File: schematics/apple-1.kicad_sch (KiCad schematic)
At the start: 9 parts, among them SW1 SW_Push, U1 W65C02SxP, U2 28C256, U3 74HC138, U4 CY62256-70PC, U5 W65C21SxP, U6 74HC04

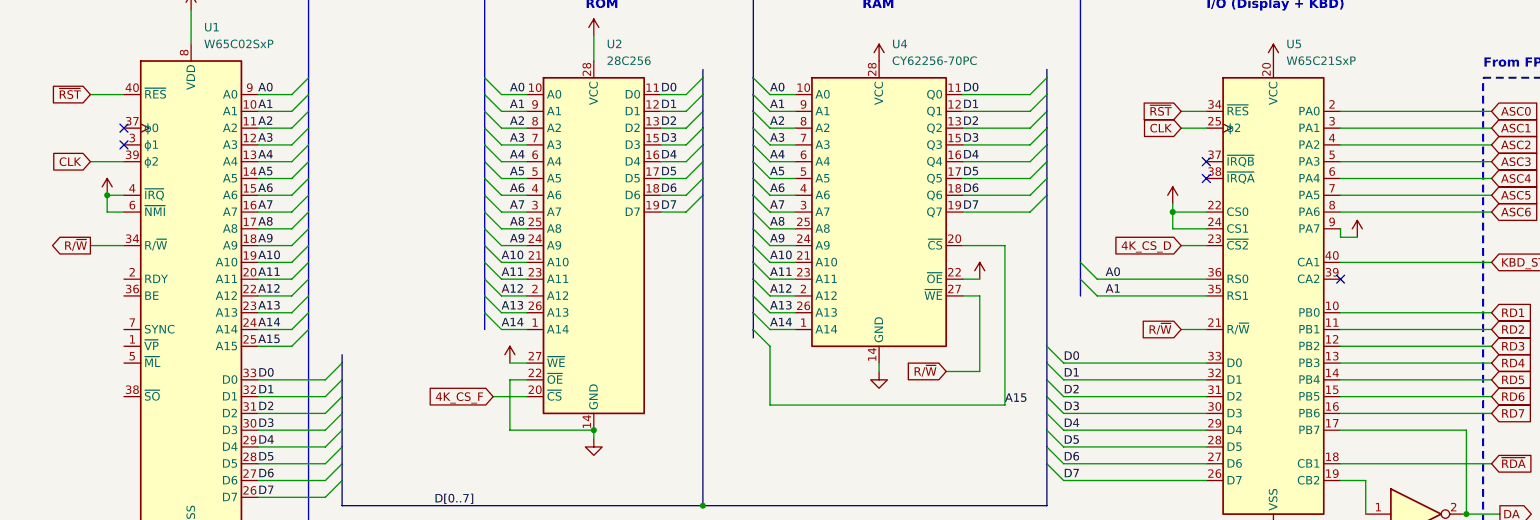
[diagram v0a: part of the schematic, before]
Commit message: updated schematics
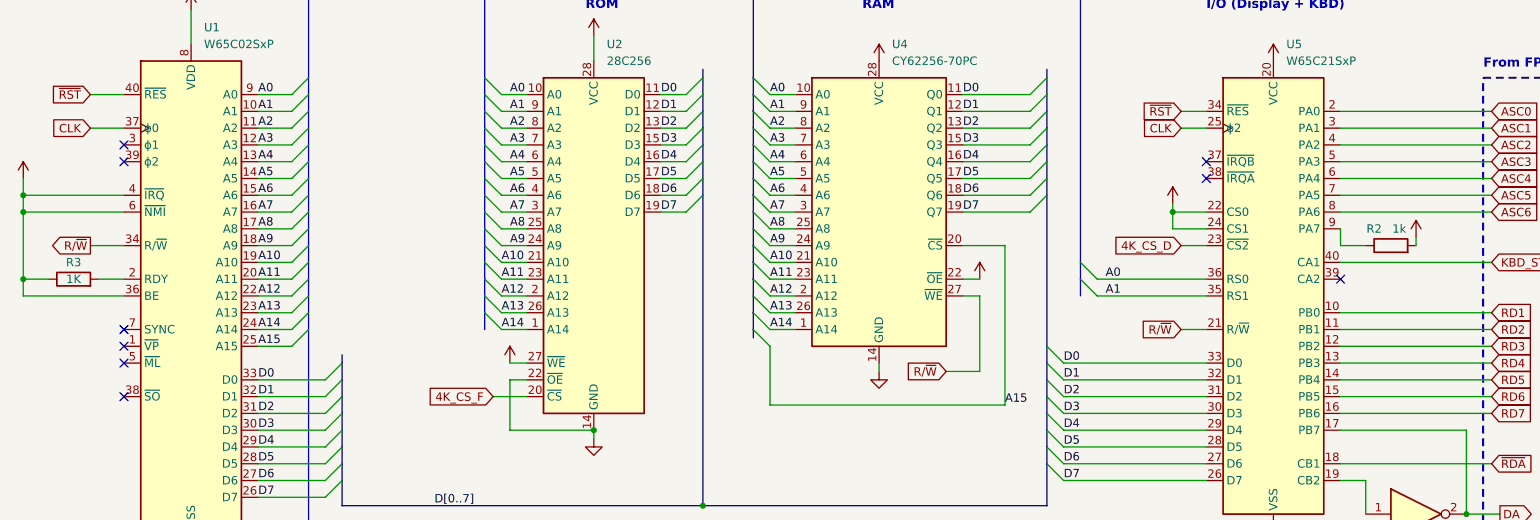
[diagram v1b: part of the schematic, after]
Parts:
- added R2: 1k, symbol Device:R
- added R3: 1K, symbol Device:R
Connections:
- net CLK: now also U1.37 (ϕ0); no longer U1.39 (ϕ2)
- net VCC: now also U1.36 (BE), R2.2, R3.1; no longer U5.9 (PA7)
- net at U1.2 (RDY): now also R3.2
- new net: R2.1, U5.9 (PA7)
- no-connect marks 5 -> 9

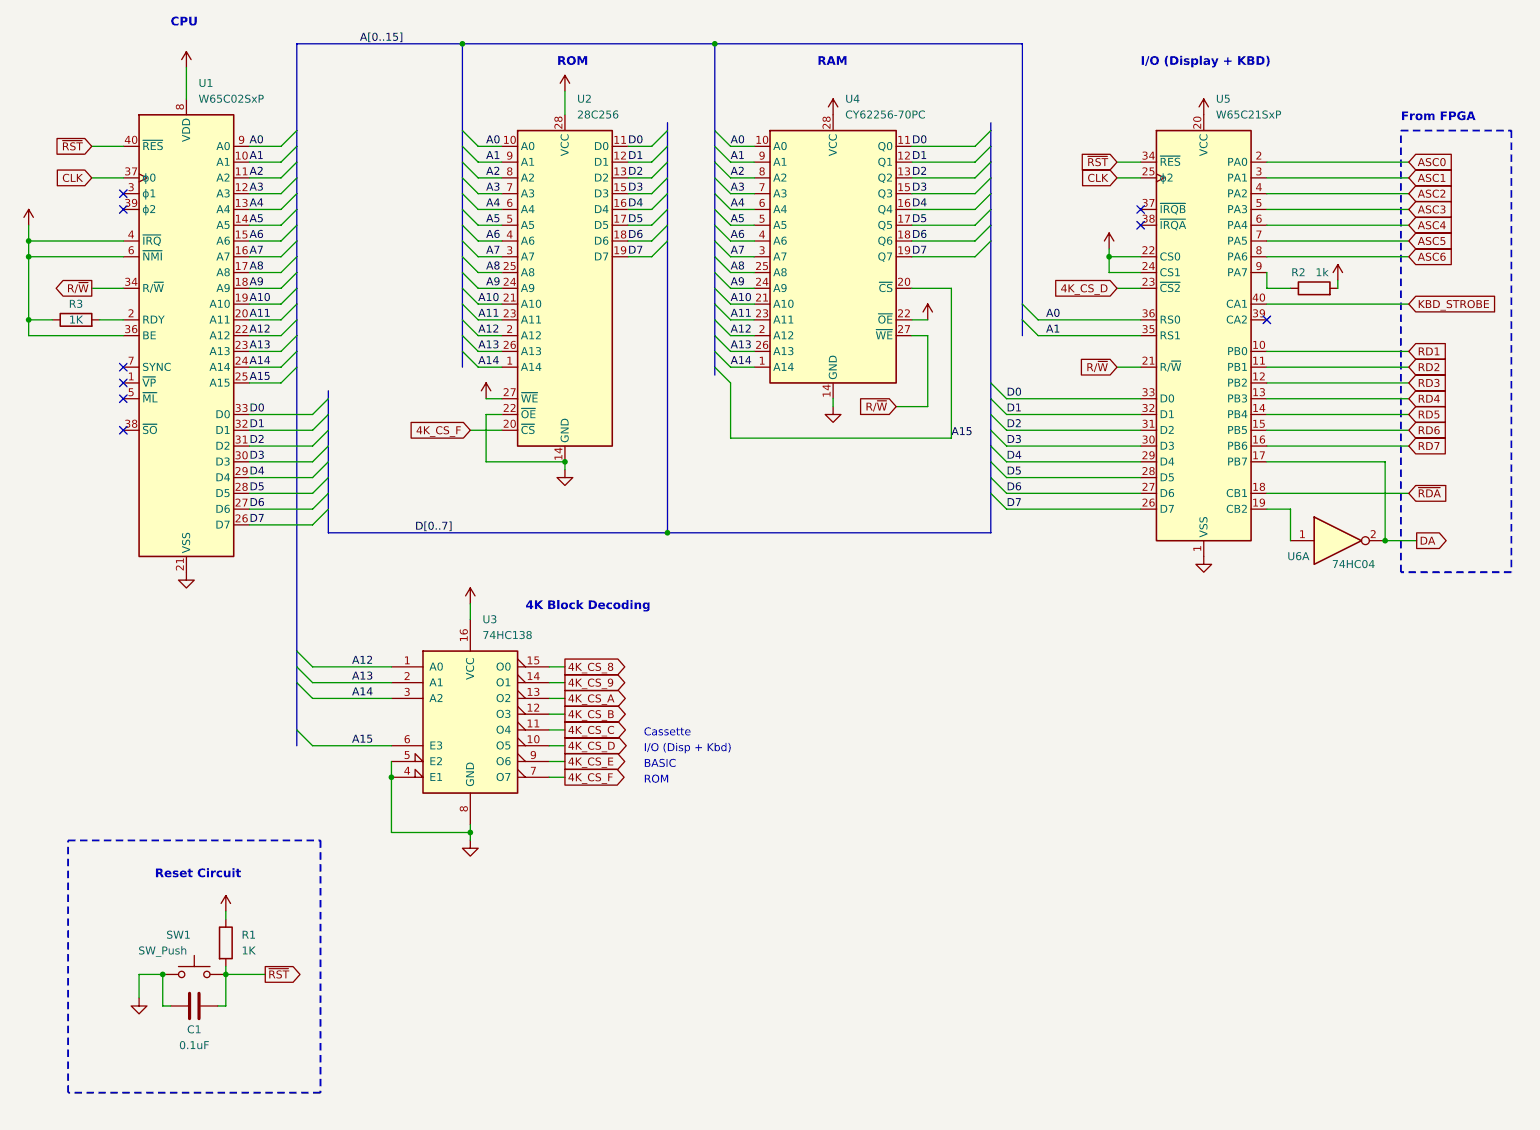
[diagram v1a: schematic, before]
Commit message: added first batch of ACI files
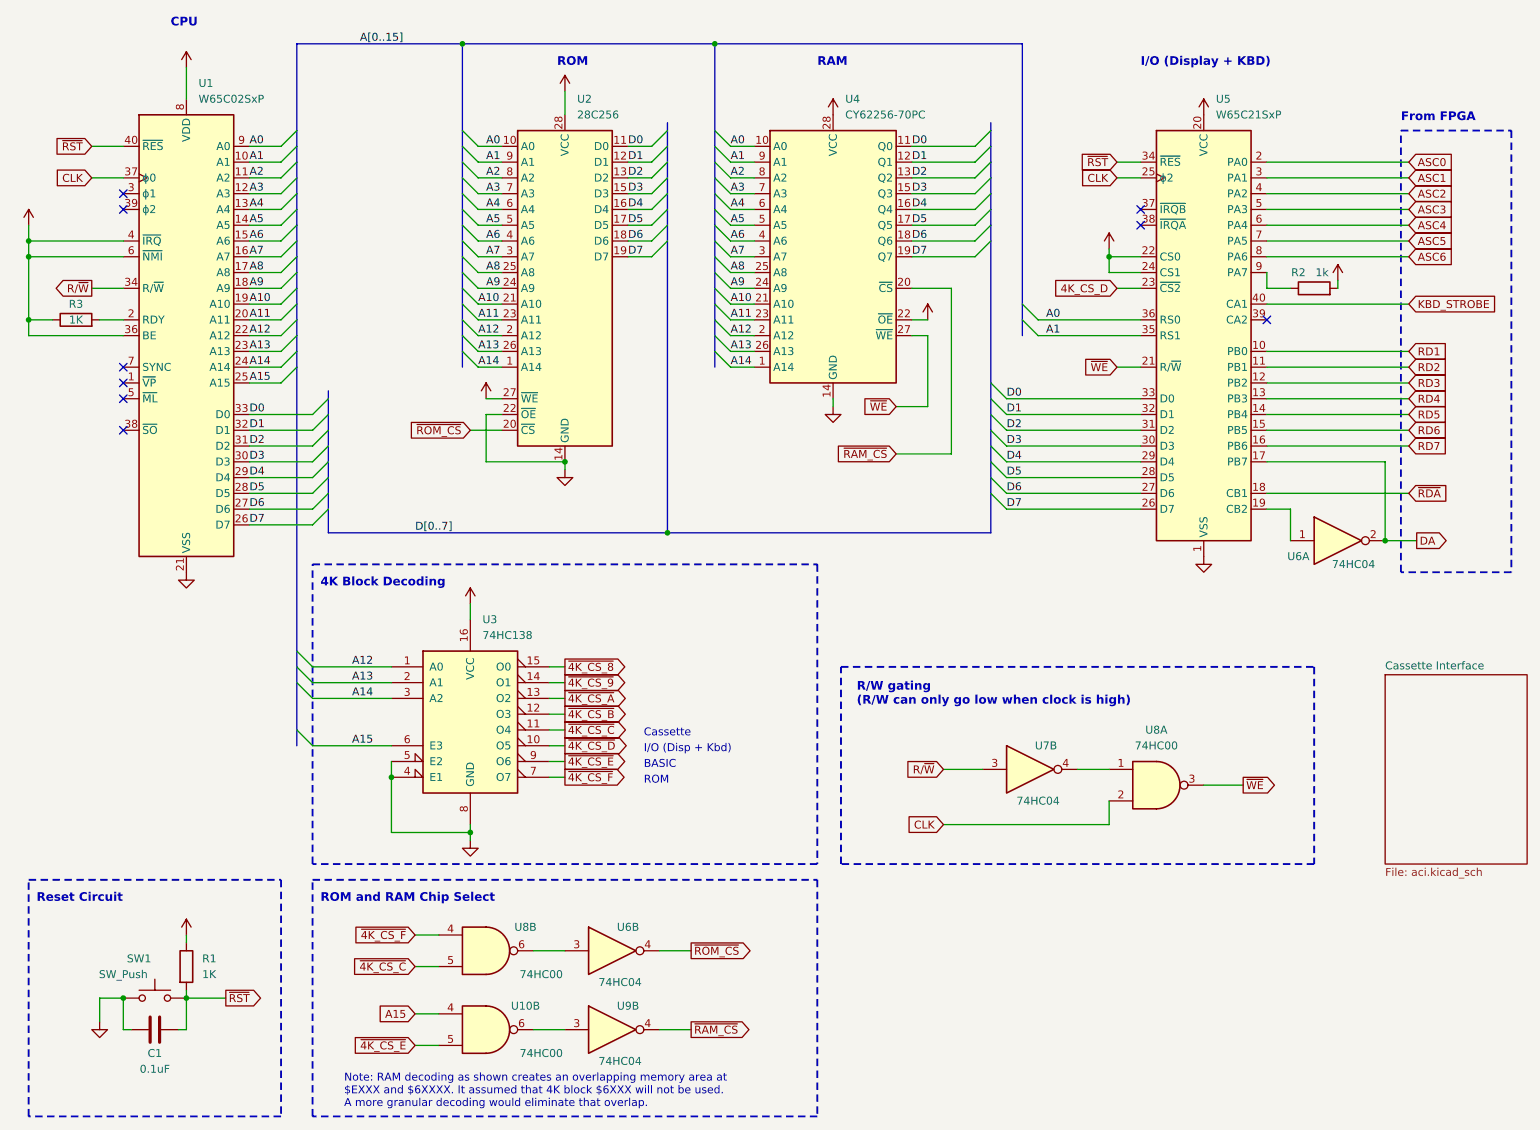
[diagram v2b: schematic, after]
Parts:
- added U10, U8: 74HC00, symbol 74xx:74HC00
- added unit 2 of U6
- added U7, U9: 74HC04, symbol 74xx:74HC04
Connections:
- net 4K_CS_D: no longer U3.10 (O5)
- net A15: now also U10.4; no longer U4.20 (~{CS})
- net CLK: now also U8.2
- net R/~{W}: now also U7.3; no longer U4.27 (~{WE}), U5.21 (R/~{W})
- net 4K_CS_8 renamed ~{4K_CS_8}
- net 4K_CS_9 renamed ~{4K_CS_9}
- net 4K_CS_A renamed ~{4K_CS_A}
- net 4K_CS_B renamed ~{4K_CS_B}
- net 4K_CS_C renamed ~{4K_CS_C}
- net ~{4K_CS_C}: now also U8.5
- net 4K_CS_E renamed ~{4K_CS_E}
- net ~{4K_CS_E}: now also U10.5
- net 4K_CS_F renamed ~{4K_CS_F}
- net ~{4K_CS_F}: now also U8.4; no longer U2.20 (~{CS})
- new net: U10.6, U9.3
- new net: U7.4, U8.1
- new net: U6.3, U8.6
- new net ~{4K_CS_D}: U3.10 (O5)
- new net ~{RAM_CS}: U4.20 (~{CS}), U9.4
- new net ~{ROM_CS}: U2.20 (~{CS}), U6.4
- new net ~{WE}: U4.27 (~{WE}), U5.21 (R/~{W}), U8.3
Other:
- added sheet Cassette Interface (aci.kicad_sch)
- note added: "Note: RAM decoding as shown creates an overlapping memory area at $EXXX and $6XXXX. It assumed that 4K block $6XXX will not be used. A more granular decoding would eliminate that overlap."
- note added: "R/W gating (R/W can only go low when clock is high)"
- note added: "ROM and RAM Chip Select"
- moved on the sheet: C1, R1, SW1

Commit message: added UART to design
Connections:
- net GND: no longer U2.22 (~{OE})
- net ~{R}/W: now reaches U7.4, U8.1
- net ~{R}/W: now also U2.22 (~{OE})
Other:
- added sheet IEC Interface (iec_interface.kicad_sch)
- added sheet UART (uart.kicad_sch)
- added sheet UART-FPGA (uart-fpga.kicad_sch)
- note added: "Apple 1 on Breadboard Project"
- note added: "I/O IEC Disk"
- moved on the sheet: U7B, U8A
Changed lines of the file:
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@@
   (junction (at 43.18 180.34) (diameter 0) (color 0 0 0 0)
   )
+  (junction (at 189.23 147.32) (diameter 0) (color 0 0 0 0)
+  )
   (junction (at 236.22 106.68) (diameter 0) (color 0 0 0 0)
-  )
-  (junction (at 104.14 93.98) (diameter 0) (color 0 0 0 0)
   )
   (junction (at 33.02 180.34) (diameter 0) (color 0 0 0 0)
@@
     (stroke (width 0) (type default))
   )
+  (wire (pts (xy 189.23 137.16) (xy 189.23 147.32))
+    (stroke (width 0) (type default))
+  )
   (wire (pts (xy 217.17 83.82) (xy 240.03 83.82))
     (stroke (width 0) (type default))
@@
     (stroke (width 0) (type default))
   )
-  (wire (pts (xy 93.98 86.36) (xy 91.44 86.36))
+  (wire (pts (xy 88.9 86.36) (xy 93.98 86.36))
     (stroke (width 0) (type default))
   )
@@
     (stroke (width 0) (type default))
   )
-  (wire (pts (xy 165.1 152.4) (xy 191.77 152.4))
+  (wire (pts (xy 165.1 156.21) (xy 191.77 156.21))
     (stroke (width 0) (type default))
   )
@@
     (stroke (width 0) (type default))
   )
+  (wire (pts (xy 191.77 137.16) (xy 189.23 137.16))
+    (stroke (width 0) (type default))
+  )
   (bus (pts (xy 66.04 86.36) (xy 66.04 88.9))
     (stroke (width 0) (type default))
@@
     (stroke (width 0) (type default))
   )
-  (wire (pts (xy 207.01 146.05) (xy 213.36 146.05))
+  (wire (pts (xy 207.01 149.86) (xy 213.36 149.86))
     (stroke (width 0) (type default))
   )
@@
     (stroke (width 0) (type default))
   )
-  (wire (pts (xy 191.77 152.4) (xy 191.77 148.59))
+  (wire (pts (xy 191.77 156.21) (xy 191.77 152.4))
     (stroke (width 0) (type default))
   )
@@
     (stroke (width 0) (type default))
   )
-  (wire (pts (xy 91.44 93.98) (xy 104.14 93.98))
-    (stroke (width 0) (type default))
-  )
   (wire (pts (xy 130.81 55.88) (xy 134.62 55.88))
     (stroke (width 0) (type default))
@@
     (stroke (width 0) (type default))
   )
-  (wire (pts (xy 91.44 86.36) (xy 91.44 93.98))
-    (stroke (width 0) (type default))
-  )
   (wire (pts (xy 130.81 50.8) (xy 134.62 50.8))
     (stroke (width 0) (type default))
@@
     (stroke (width 0) (type default))
   )
-  (wire (pts (xy 186.69 143.51) (xy 191.77 143.51))
+  (wire (pts (xy 186.69 147.32) (xy 189.23 147.32))
     (stroke (width 0) (type default))
   )
@@
     (stroke (width 0) (type default))
   )
-  (wire (pts (xy 165.1 143.51) (xy 171.45 143.51))
+  (wire (pts (xy 165.1 147.32) (xy 171.45 147.32))
     (stroke (width 0) (type default))
   )
@@
   )
   (bus (pts (xy 172.72 96.52) (xy 172.72 99.06))
+    (stroke (width 0) (type default))
+  )
+  (wire (pts (xy 189.23 147.32) (xy 191.77 147.32))
     (stroke (width 0) (type default))
   )
@@
     (fill (type none))
   )
+  (text "Apple 1 on Breadboard Project" (at 240.03 181.61 0)
+    (effects (font (size 2.54 2.54) (thickness 0.508) bold) (justify right bottom))
+  )
   (text "BASIC" (at 116.84 143.51 0)
+    (effects (font (size 1.27 1.27)) (justify left bottom))
+  )
+  (text "I/O IEC Disk" (at 116.84 135.89 0)
     (effects (font (size 1.27 1.27)) (justify left bottom))
   )
@@
     )
   )
-  (global_label "R{slash}~{W}" (shape input) (at 165.1 143.51 180) (fields_autoplaced)
+  (global_label "R{slash}~{W}" (shape input) (at 165.1 147.32 180) (fields_autoplaced)
     (effects (font (size 1.27 1.27)) (justify right))
-    (property "Intersheetrefs" "${INTERSHEET_REFS}" (at 158.1423 143.51 0)
+    (property "Intersheetrefs" "${INTERSHEET_REFS}" (at 158.1423 147.32 0)
       (effects (font (size 1.27 1.27)) (justify right) hide)
     )
@@
     )
   )
-  (global_label "~{WE}" (shape output) (at 213.36 146.05 0) (fields_autoplaced)
-    (effects (font (size 1.27 1.27)) (justify left))
-    (property "Intersheetrefs" "${INTERSHEET_REFS}" (at 218.8662 146.05 0)
+  (global_label "~{WE}" (shape output) (at 213.36 149.86 0) (fields_autoplaced)
+    (effects (font (size 1.27 1.27)) (justify left))
+    (property "Intersheetrefs" "${INTERSHEET_REFS}" (at 218.8662 149.86 0)
       (effects (font (size 1.27 1.27)) (justify left) hide)
     )
@@
     )
   )
-  (global_label "CLK" (shape input) (at 165.1 152.4 180) (fields_autoplaced)
+  (global_label "CLK" (shape input) (at 165.1 156.21 180) (fields_autoplaced)
     (effects (font (size 1.27 1.27)) (justify right))
-    (property "Intersheetrefs" "${INTERSHEET_REFS}" (at 158.6261 152.4 0)
+    (property "Intersheetrefs" "${INTERSHEET_REFS}" (at 158.6261 156.21 0)
       (effects (font (size 1.27 1.27)) (justify right) hide)
     )
@@
     (effects (font (size 1.27 1.27)) (justify left))
     (property "Intersheetrefs" "${INTERSHEET_REFS}" (at 115.1495 127 0)
+      (effects (font (size 1.27 1.27)) (justify left) hide)
+    )
+  )
+  (global_label "~{R}{slash}W" (shape output) (at 191.77 137.16 0) (fields_autoplaced)
+    (effects (font (size 1.27 1.27)) (justify left))
+    (property "Intersheetrefs" "${INTERSHEET_REFS}" (at 198.7277 137.16 0)
       (effects (font (size 1.27 1.27)) (justify left) hide)
     )
@@
     (effects (font (size 1.27 1.27)) (justify right))
     (property "Intersheetrefs" "${INTERSHEET_REFS}" (at 20.9823 66.04 0)
+      (effects (font (size 1.27 1.27)) (justify right) hide)
+    )
+  )
+  (global_label "~{R}{slash}W" (shape input) (at 88.9 86.36 180) (fields_autoplaced)
+    (effects (font (size 1.27 1.27)) (justify right))
+    (property "Intersheetrefs" "${INTERSHEET_REFS}" (at 81.9423 86.36 0)
       (effects (font (size 1.27 1.27)) (justify right) hide)
     )
@@
     )
   )
-  (symbol (lib_id "74xx:74HC00") (at 199.39 146.05 0) (unit 1)
+  (symbol (lib_id "74xx:74HC00") (at 199.39 149.86 0) (unit 1)
     (in_bom yes) (on_board yes) (dnp no) (fields_autoplaced)
-    (property "Reference" "U8" (at 199.3817 137.16 0)
+    (property "Reference" "U8" (at 199.3817 140.97 0)
       (effects (font (size 1.27 1.27)))
     )
-    (property "Value" "74HC00" (at 199.3817 139.7 0)
+    (property "Value" "74HC00" (at 199.3817 143.51 0)
       (effects (font (size 1.27 1.27)))
     )
-    (property "Footprint" "" (at 199.39 146.05 0)
-      (effects (font (size 1.27 1.27)) hide)
-    )
-    (property "Datasheet" "http://www.ti.com/lit/gpn/sn74hc00" (at 199.39 146.05 0)
+    (property "Footprint" "" (at 199.39 149.86 0)
+      (effects (font (size 1.27 1.27)) hide)
+    )
+    (property "Datasheet" "http://www.ti.com/lit/gpn/sn74hc00" (at 199.39 149.86 0)
       (effects (font (size 1.27 1.27)) hide)
     )
@@
     )
   )
-  (symbol (lib_id "74xx:74HC04") (at 179.07 143.51 0) (unit 2)
+  (symbol (lib_id "74xx:74HC04") (at 179.07 147.32 0) (unit 2)
     (in_bom yes) (on_board yes) (dnp no)
-    (property "Reference" "U7" (at 181.61 139.7 0)
+    (property "Reference" "U7" (at 181.61 143.51 0)
       (effects (font (size 1.27 1.27)))
     )
-    (property "Value" "74HC04" (at 180.34 148.59 0)
+    (property "Value" "74HC04" (at 180.34 152.4 0)
       (effects (font (size 1.27 1.27)))
     )
-    (property "Footprint" "" (at 179.07 143.51 0)
-      (effects (font (size 1.27 1.27)) hide)
-    )
-    (property "Datasheet" "https://assets.nexperia.com/documents/data-sheet/74HC_HCT04.pdf" (at 179.07 143.51 0)
+    (property "Footprint" "" (at 179.07 147.32 0)
+      (effects (font (size 1.27 1.27)) hide)
+    )
+    (property "Datasheet" "https://assets.nexperia.com/documents/data-sheet/74HC_HCT04.pdf" (at 179.07 147.32 0)
       (effects (font (size 1.27 1.27)) hide)
     )
@@
       )
     )
+  )
+  (sheet (at 15.24 120.65) (size 17.78 11.43) (fields_autoplaced)
+    (stroke (width 0.1524) (type solid))
+    (fill (color 0 0 0 0.0000))
+    (property "Sheetname" "UART" (at 15.24 119.9384 0)
+      (effects (font (size 1.27 1.27)) (justify left bottom))
+    )
+    (property "Sheetfile" "uart.kicad_sch" (at 15.24 132.6646 0)
+      (effects (font (size 1.27 1.27)) (justify left top))
+    )
+    (instances
+      (project "apple-1"
+        (path "/49da186c-18fb-4ced-8737-786ea50767d0" (page "4"))
+      )
+    )
+  )
+  (sheet (at 15.24 139.7) (size 22.86 11.43) (fields_autoplaced)
+    (stroke (width 0.1524) (type solid))
+    (fill (color 0 0 0 0.0000))
+    (property "Sheetname" "IEC Interface" (at 15.24 138.9884 0)
+      (effects (font (size 1.27 1.27)) (justify left bottom))
+    )
+    (property "Sheetfile" "iec_interface.kicad_sch" (at 15.24 151.7146 0)
+      (effects (font (size 1.27 1.27)) (justify left top))
+    )
+    (instances
+      (project "apple-1"
+        (path "/49da186c-18fb-4ced-8737-786ea50767d0" (page "3"))
+      )
+    )
+  )
+  (sheet (at 15.24 102.87) (size 12.7 11.43) (fields_autoplaced)
+    (stroke (width 0.1524) (type solid))
+    (fill (color 0 0 0 0.0000))
+    (property "Sheetname" "UART-FPGA" (at 15.24 102.1584 0)
+      (effects (font (size 1.27 1.27)) (justify left bottom))
+    )
+    (property "Sheetfile" "uart-fpga.kicad_sch" (at 15.24 114.8846 0)
+      (effects (font (size 1.27 1.27)) (justify left top))
+    )
+    (instances
+      (project "apple-1"
+        (path "/49da186c-18fb-4ced-8737-786ea50767d0" (page "5"))
+      )
+    )

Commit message: added ice40 support
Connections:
- net ~{4K_CS_C}: now also U8.13; no longer U8.5
- net ~{4K_CS_F}: now also U8.12; no longer U8.4
- net at U6.3: now also U8.11; no longer U8.6
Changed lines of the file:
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@@
     )
   )
-  (symbol (lib_id "74xx:74HC00") (at 91.44 172.72 0) (unit 2)
+  (symbol (lib_id "74xx:74HC00") (at 91.44 172.72 0) (unit 4)
     (in_bom yes) (on_board yes) (dnp no)
     (property "Reference" "U8" (at 97.79 168.91 0)
@@
       (project "apple-1"
         (path "/49da186c-18fb-4ced-8737-786ea50767d0"
-          (reference "U8") (unit 2)
+          (reference "U8") (unit 4)
         )
       )
